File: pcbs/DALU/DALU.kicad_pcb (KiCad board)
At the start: 4 copper layers, 73 parts, among them J201 Conn_02x20_Odd_Even, U201 74HC245, U202 74HC245, U203 74HC245, U301 74HC138, U401 74HC86, U402 74HC86, U403 74HC86, U404 74HC08, U405 74HC283, U406 74HC283, U407 74HC245, U408 74HC245, U501 74HC00, U502 74HC00, U503 74HC14, U504 74HC14, U505 74HC245, U506 74HC245, U601 74HC86, U602 74HC86, U603 74HC245, U701 74HC245, U801 74HC74, U802 74HCT574

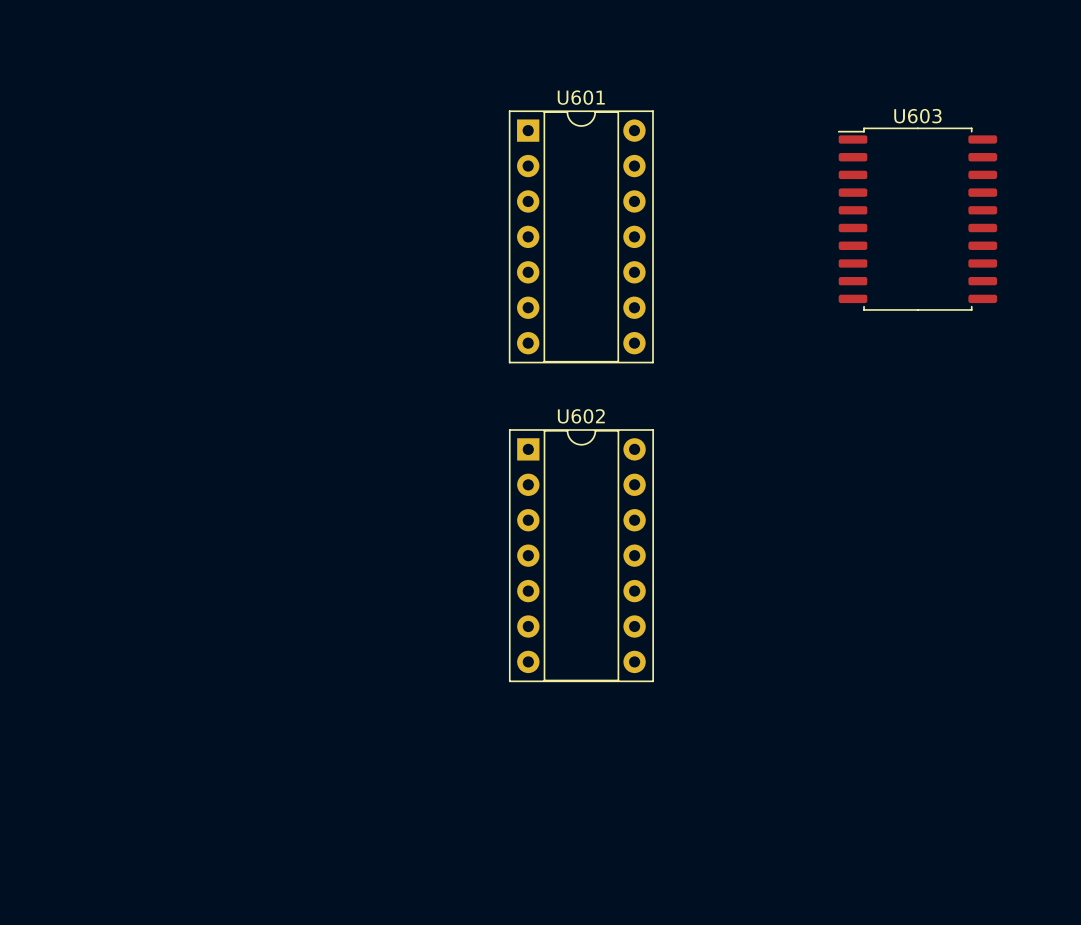
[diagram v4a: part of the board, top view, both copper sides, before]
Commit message: Routing the XOR
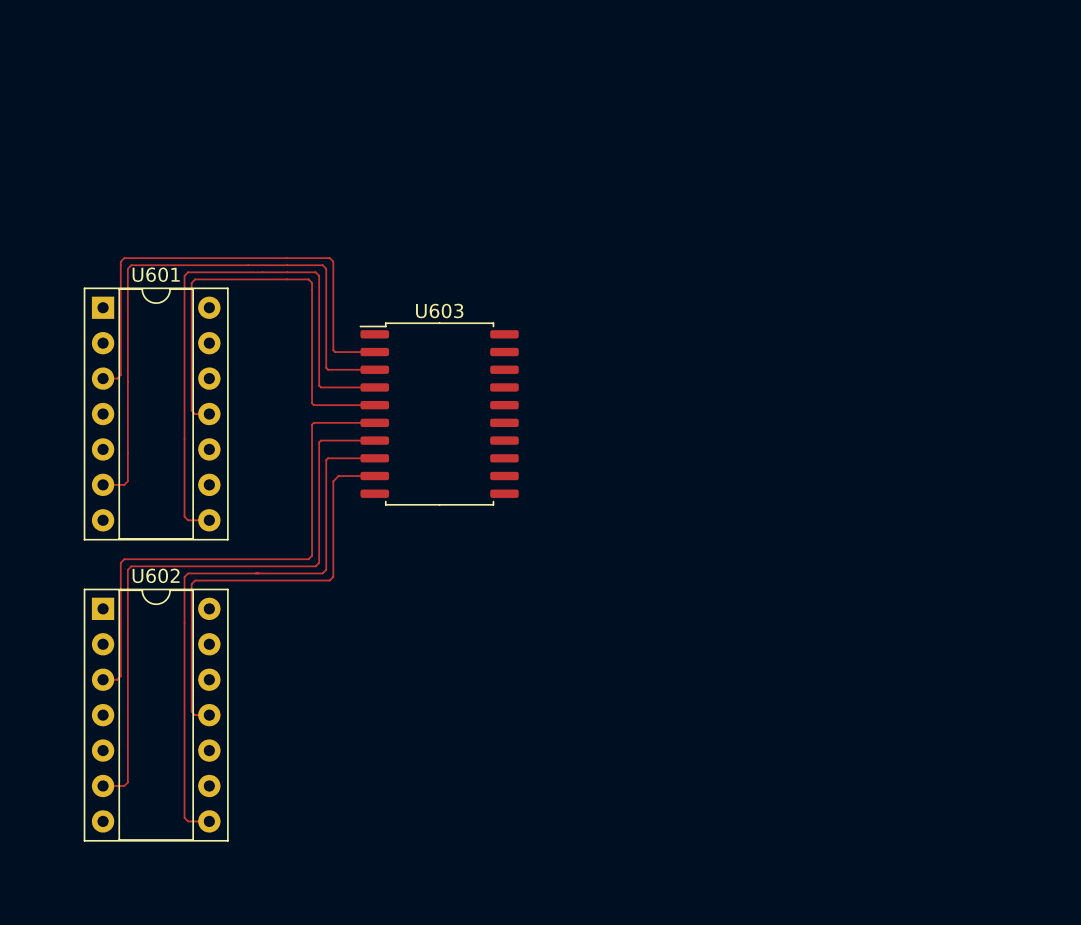
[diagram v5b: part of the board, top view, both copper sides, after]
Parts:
- moved U603 37.0 mm to (162.6, 54.6)
- moved U601 33.0 mm to (138.4, 47.0)
- moved U602 32.6 mm to (138.4, 68.6)
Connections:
- net Net-(U601-Pad3) renamed /XOR/XOR0
- net Net-(U601-Pad6) renamed /XOR/XOR1
- net Net-(U602-Pad3) renamed /XOR/XOR4
- net Net-(U602-Pad6) renamed /XOR/XOR5
- U601 pad 10: /AND-NAND/B3 -> /AND-NAND/B2
- U601 pad 11: Net-(U601-Pad11) -> /XOR/XOR3
- U601 pad 12: /AND-NAND/A2 -> /AND-NAND/A3
- U601 pad 13: /AND-NAND/B2 -> /AND-NAND/B3
- U601 pad 8: Net-(U601-Pad8) -> /XOR/XOR2
- U601 pad 9: /AND-NAND/A3 -> /AND-NAND/A2
- U602 pad 10: /AND-NAND/B7 -> /AND-NAND/B6
- U602 pad 11: Net-(U602-Pad11) -> /XOR/XOR7
- U602 pad 12: /AND-NAND/A6 -> /AND-NAND/A7
- U602 pad 13: /AND-NAND/B6 -> /AND-NAND/B7
- U602 pad 8: Net-(U602-Pad8) -> /XOR/XOR6
- U602 pad 9: /AND-NAND/A7 -> /AND-NAND/A6
- U603 pad 4: Net-(U601-Pad11) -> /XOR/XOR2
- U603 pad 5: Net-(U601-Pad8) -> /XOR/XOR3
- U603 pad 8: Net-(U602-Pad11) -> /XOR/XOR6
- U603 pad 9: Net-(U602-Pad8) -> /XOR/XOR7
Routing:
- net /AND-NAND/A0: track 76.4 -> 121.2 mm
- net /XOR/XOR5: track 0.00 -> 43.7 mm
- net /XOR/XOR1: track 0.00 -> 42.2 mm
- net /AND-NAND/B3: track 119.6 -> 161.6 mm
- net /AND-NAND/B0: track 110.2 -> 152.2 mm
- net /XOR/XOR6: track 0.00 -> 41.2 mm
- net /XOR/XOR2: track 0.00 -> 40.9 mm
- net /AND-NAND/A3: track 78.4 -> 118.1 mm
- net /XOR/XOR4: track 0.00 -> 37.4 mm
- net /AND-NAND/A1: track 85.3 -> 122.0 mm
- net /AND-NAND/B1: track 122.9 -> 157.5 mm
- net /XOR/XOR0: track 0.00 -> 34.3 mm
- net /AND-NAND/B2: track 125.2 -> 159.3 mm
- net /XOR/XOR3: track 0.00 -> 32.5 mm
- net /AND-NAND/A2: track 107.4 -> 139.0 mm
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
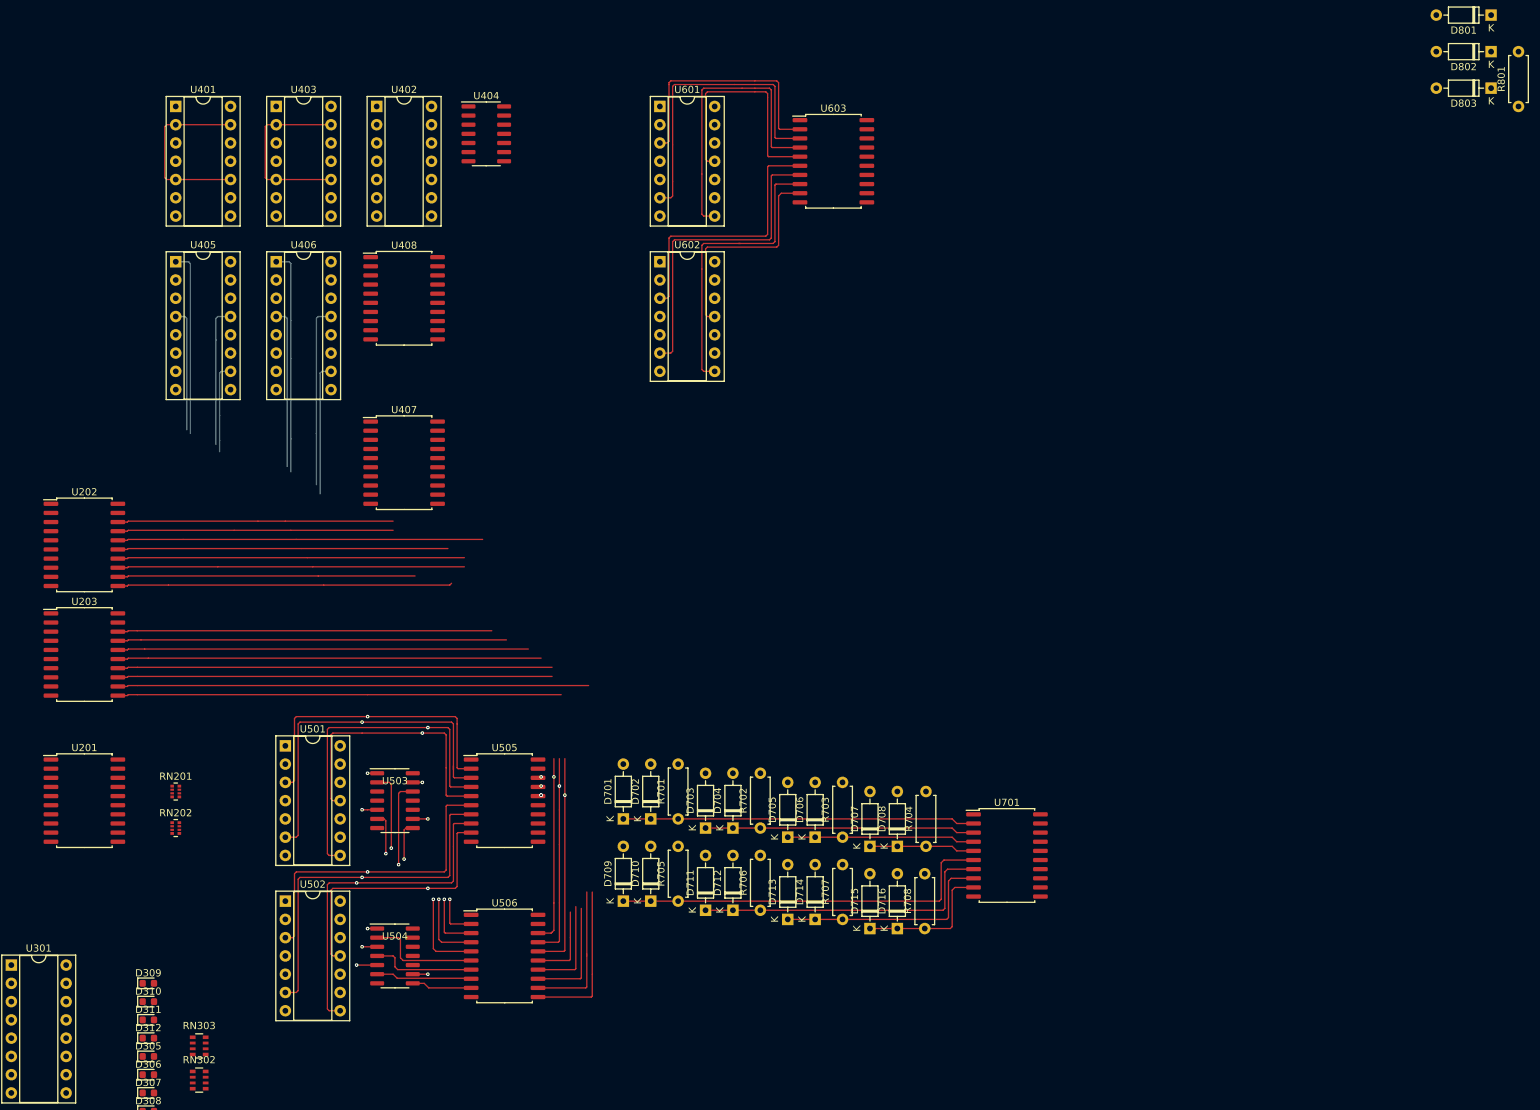
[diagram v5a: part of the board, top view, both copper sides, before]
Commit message: Removing diode ORs (mainly). Preparing for a small rethink
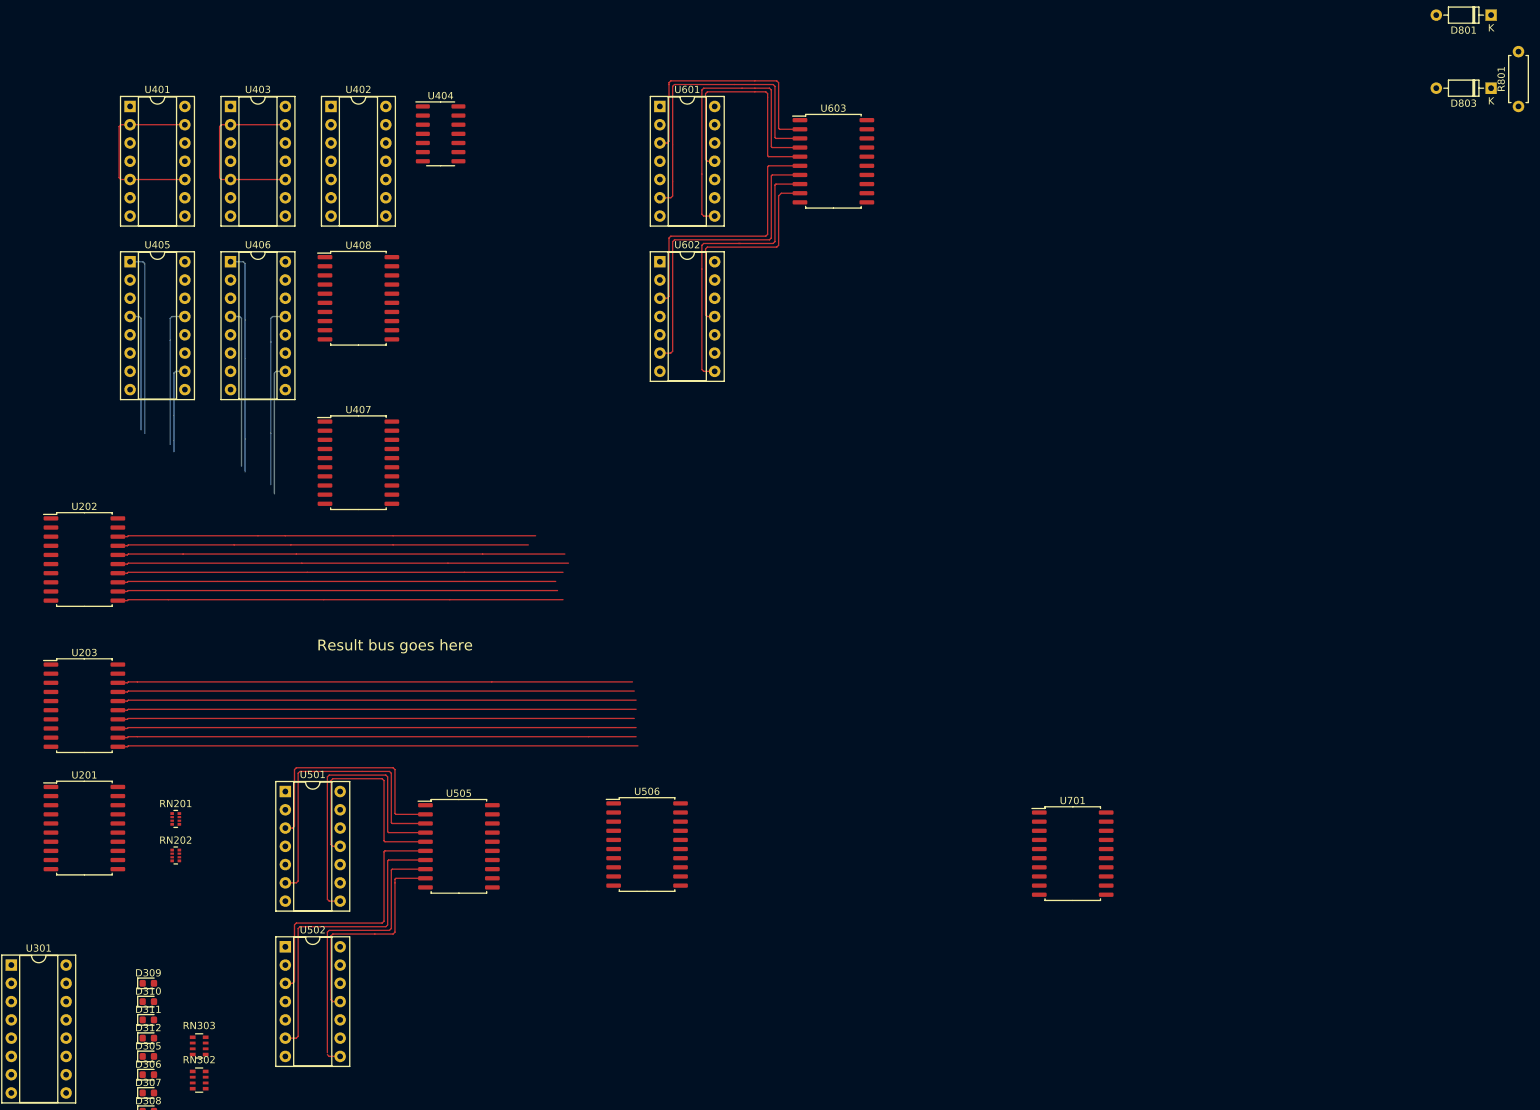
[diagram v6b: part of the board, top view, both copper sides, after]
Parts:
- removed D701, D702, D703, D704, D705, D706, D707, D708, D709, D710, D711, D712, D713, D714, D715, D716, D802: 1N4148, Diode_THT:D_DO-35_SOD27_P7.62mm_Horizontal
- removed R701, R702, R703, R704, R705, R706, R707, R708: 100k, Resistor_THT:R_Axial_DIN0207_L6.3mm_D2.5mm_P7.62mm_Horizontal
- removed U503, U504: 74HC14, Package_SO:SOIC-14_3.9x8.7mm_P1.27mm
- moved U506 25.2 mm to (136.7, 149.6)
- moved U701 9.15 mm to (195.8, 150.9)
- moved U505 8.98 mm to (110.5, 149.9)
- moved U203 7.11 mm to (58.4, 130.3)
- moved U501 6.35 mm to (86.4, 142.2)
- moved U502 6.35 mm to (86.4, 163.8)
- moved U401 6.35 mm to (64.8, 47.0)
- moved U402 6.35 mm to (92.7, 47.0)
- moved U403 6.35 mm to (78.7, 47.0)
- moved U405 6.35 mm to (64.8, 68.6)
- moved U406 6.35 mm to (78.7, 68.6)
- moved U407 6.35 mm to (96.5, 96.5)
- moved U408 6.35 mm to (96.5, 73.7)
- moved U404 6.35 mm to (108.0, 50.8)
- moved RN201 3.81 mm to (71.1, 146.1)
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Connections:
- U506 pad 2: /AND-NAND/AND0 -> unconnected-(U506-Pad2)
- U506 pad 3: /AND-NAND/AND1 -> unconnected-(U506-Pad3)
- U506 pad 4: /AND-NAND/AND2 -> unconnected-(U506-Pad4)
- U506 pad 5: /AND-NAND/AND3 -> unconnected-(U506-Pad5)
- U506 pad 6: /AND-NAND/AND4 -> unconnected-(U506-Pad6)
- U506 pad 7: /AND-NAND/AND5 -> unconnected-(U506-Pad7)
- U506 pad 8: /AND-NAND/AND6 -> unconnected-(U506-Pad8)
- U701 pad 2: Net-(D701-Pad1) -> unconnected-(U701-Pad2)
- U701 pad 3: Net-(D703-Pad1) -> unconnected-(U701-Pad3)
- U701 pad 4: Net-(D705-Pad1) -> unconnected-(U701-Pad4)
- U701 pad 5: Net-(D707-Pad1) -> unconnected-(U701-Pad5)
- U701 pad 6: Net-(D709-Pad1) -> unconnected-(U701-Pad6)
- U701 pad 7: Net-(D711-Pad1) -> unconnected-(U701-Pad7)
- U701 pad 8: Net-(D713-Pad1) -> unconnected-(U701-Pad8)
- U701 pad 9: Net-(D715-Pad1) -> unconnected-(U701-Pad9)
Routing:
- net Net-(D709-Pad1): track 54.0 -> 0.00 mm
- net Net-(D701-Pad1): track 49.0 -> 0.00 mm
- net Net-(D711-Pad1): track 42.6 -> 0.00 mm
- net Net-(D703-Pad1): track 37.5 -> 0.00 mm
- net /AND-NAND/RESULT2: track 33.8 -> 0.00 mm, vias 3 -> 0
- net /AND-NAND/AND3: track 33.8 -> 0.00 mm, vias 2 -> 0
- net /AND-NAND/AND0: track 32.4 -> 0.00 mm, vias 2 -> 0
- net Net-(D713-Pad1): track 31.2 -> 0.00 mm
- net /AND-NAND/RESULT1: track 31.0 -> 0.00 mm, vias 2 -> 0
- net /AND-NAND/AND1: track 28.6 -> 0.00 mm, vias 2 -> 0
- net /AND-NAND/RESULT0: track 28.0 -> 0.00 mm, vias 2 -> 0
- net Net-(D705-Pad1): track 26.1 -> 0.00 mm
- net /AND-NAND/AND2: track 25.9 -> 0.00 mm, vias 2 -> 0
- net /AND-NAND/NAND1: track 63.9 -> 41.7 mm, vias 2 -> 0
- net /AND-NAND/RESULT7: track 22.1 -> 0.00 mm
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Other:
- board text added: "Result bus goes here"
